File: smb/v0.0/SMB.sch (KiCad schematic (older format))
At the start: 25 parts, among them IC101 ATMEGA1284-A, J102 RTS_RESET, J103 ICSP, J104 SERIAL_REV, P101 I2C_CONN, P102 CONN_6, P103 CONN_5X2, P104 CONN_5X2, SW101 SKQGAKE010, X101 16MHz

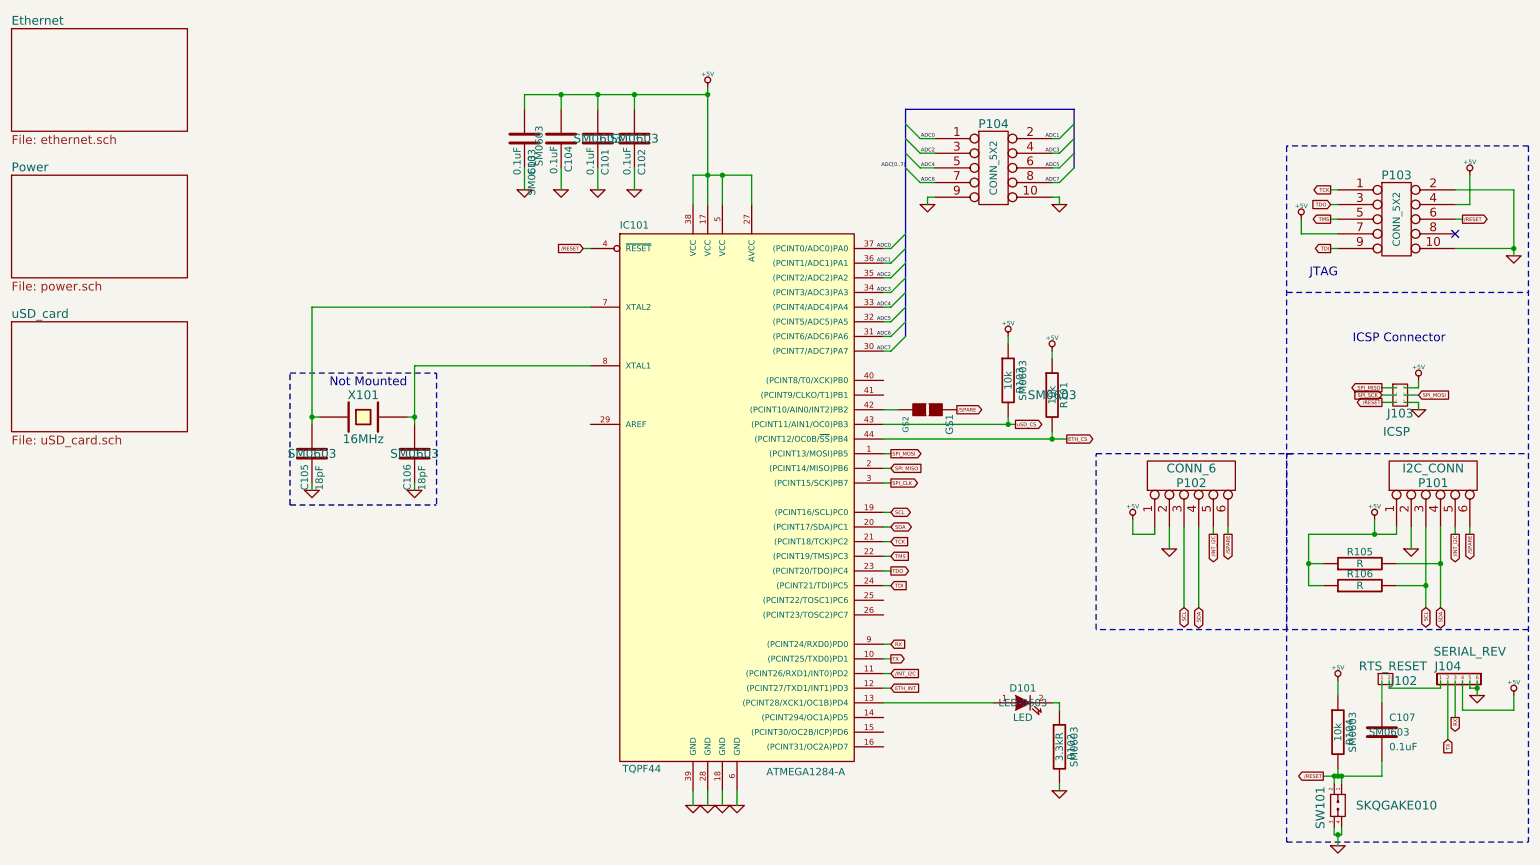
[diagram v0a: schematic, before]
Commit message: Corrected production mistakes. SPI_CLK for ISP, MISO sdcard
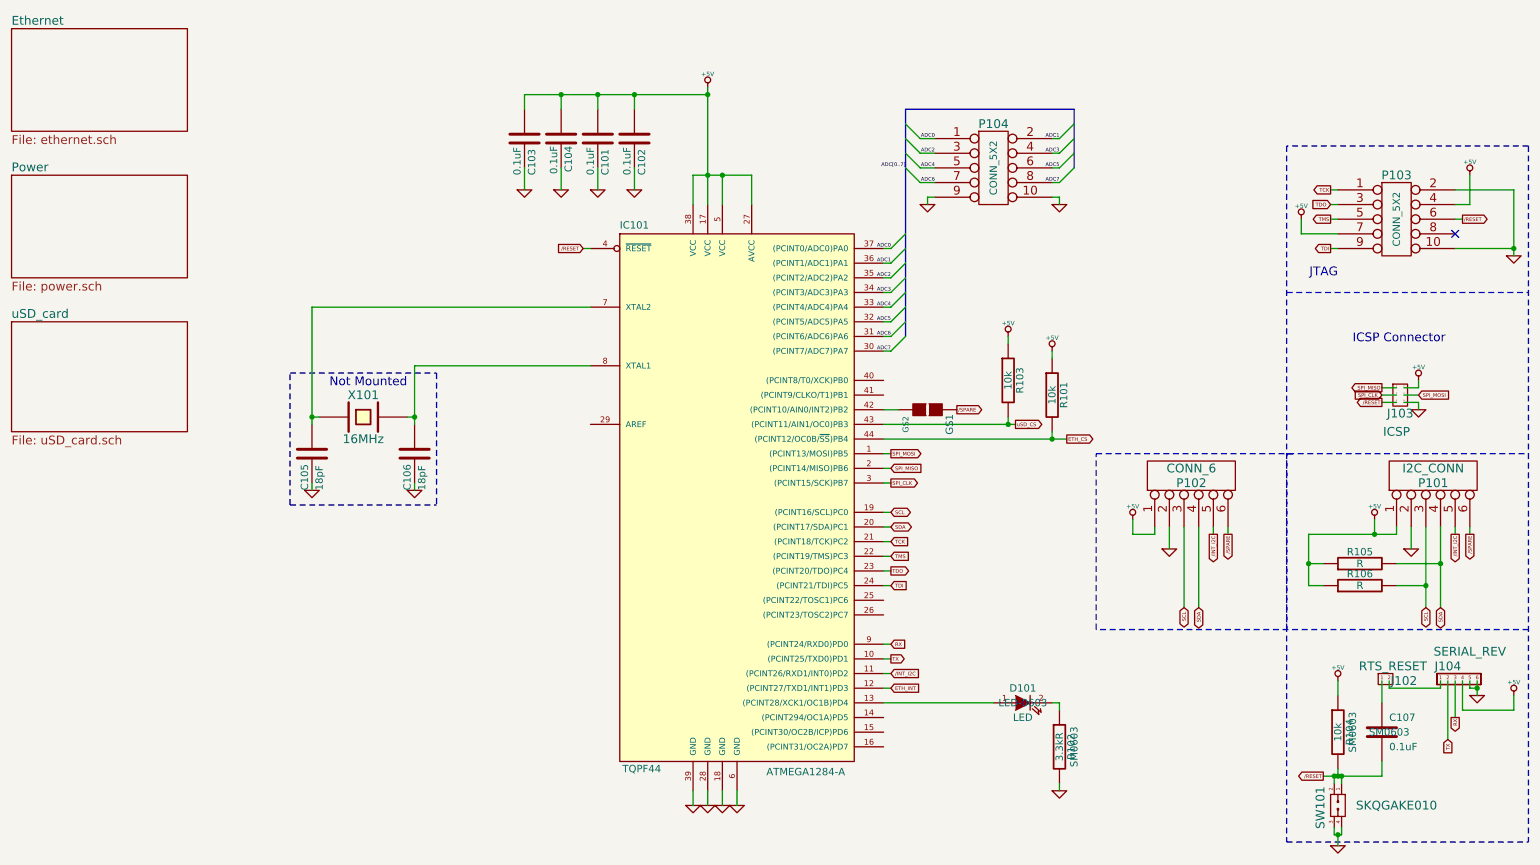
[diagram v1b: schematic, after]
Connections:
- net SPI_SCK is gone; now on net SPI_CLK: J103.3
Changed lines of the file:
@@
-EESchema Schematic File Version 2  date jeu. 13 sept. 2012 22:24:34 CEST
+EESchema Schematic File Version 2  date 10/02/2013 13:01:35
 LIBS:power
 LIBS:device
@@
 EELAYER 25  0
 EELAYER END
-$Descr A4 11693 8268
+$Descr A4 11700 8267
 encoding utf-8
 Sheet 1 4
 Title "Short Main Board - SMB controller"
-Date "10 sep 2012"
+Date "10 feb 2013"
 Rev "0"
 Comp "XPLDUINO project"
@@
 F 0 "R103" V 7480 3000 50  0000 C CNN
 F 1 "10k" V 7400 3000 50  0000 C CNN
-F 2 "SM0603" V 7500 3000 50  0000 C CNN
+F 2 "SM0603" V 7500 3000 50  0001 C CNN
 	1    7400 3000
 	1    0    0    -1
@@
 /RESET
 Text GLabel 9950 3100 0    25   Input ~ 0
-SPI_SCK
+SPI_CLK
 Text GLabel 10200 3100 2    25   Input ~ 0
 SPI_MOSI
@@
 F 0 "C103" V 4150 1100 50  0000 L CNN
 F 1 "0.1uF" V 4050 1100 50  0000 L CNN
-F 2 "SM0603" V 4150 1100 50  0000 C CNN
+F 2 "SM0603" V 4150 1100 50  0001 C CNN
 	1    4100 1350
 	1    0    0    -1
@@
 F 0 "R101" V 7780 3100 50  0000 C CNN
 F 1 "10k" V 7700 3100 50  0000 C CNN
-F 2 "SM0603" H 7700 3100 60  0000 C CNN
+F 2 "SM0603" H 7700 3100 60  0001 C CNN
 	1    7700 3100
 	1    0    0    -1
@@
 F 0 "C104" V 4300 1400 50  0000 L CNN
 F 1 "0.1uF" V 4400 1400 50  0000 L CNN
-F 2 "SM0603" V 4500 1400 50  0000 C CNN
+F 2 "SM0603" V 4500 1400 50  0001 C CNN
 	1    4350 1350
 	-1   0    0    1
@@
 F 0 "C106" V 3300 3250 50  0000 L CNN
 F 1 "18pF" V 3400 3250 50  0000 L CNN
-F 2 "SM0603" H 3350 3500 60  0000 C CNN
+F 2 "SM0603" H 3350 3500 60  0001 C CNN
 	1    3350 3500
 	1    0    0    -1
@@
 F 0 "C105" V 2600 3250 50  0000 L CNN
 F 1 "18pF" V 2700 3250 50  0000 L CNN
-F 2 "SM0603" H 2650 3500 60  0000 C CNN
+F 2 "SM0603" H 2650 3500 60  0001 C CNN
 	1    2650 3500
 	1    0    0    -1
@@
 F 0 "C102" V 4900 1100 50  0000 L CNN
 F 1 "0.1uF" V 4800 1100 50  0000 L CNN
-F 2 "SM0603" H 4850 1350 60  0000 C CNN
+F 2 "SM0603" H 4850 1350 60  0001 C CNN
 	1    4850 1350
 	1    0    0    -1
@@
 F 0 "C101" V 4650 1100 50  0000 L CNN
 F 1 "0.1uF" V 4550 1100 50  0000 L CNN
-F 2 "SM0603" H 4600 1350 60  0000 C CNN
+F 2 "SM0603" H 4600 1350 60  0001 C CNN
 	1    4600 1350
 	1    0    0    -1
